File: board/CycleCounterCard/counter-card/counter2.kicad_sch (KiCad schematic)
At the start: 19 parts, among them J1 Bus_Hydra_8bit, J2 74F86, J3 74F86, J4 74F86, J5 74F86, U1 74F191, U13 74F573, U2 74F573, U21 74F573, U22 74F191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

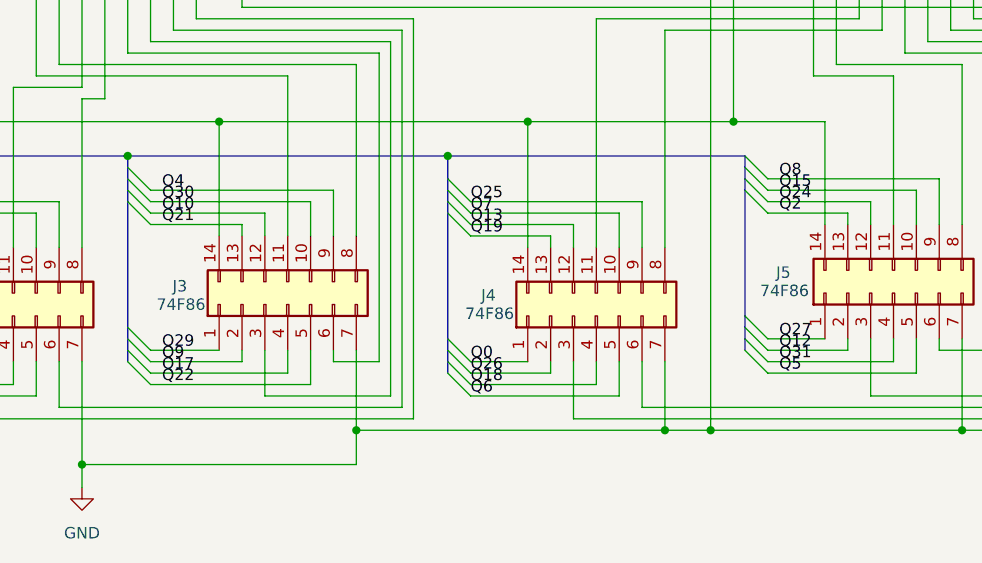
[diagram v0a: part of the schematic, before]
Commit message: Counter card updated to 4-layer to make production simpler and cheaper.  Production V1 model.
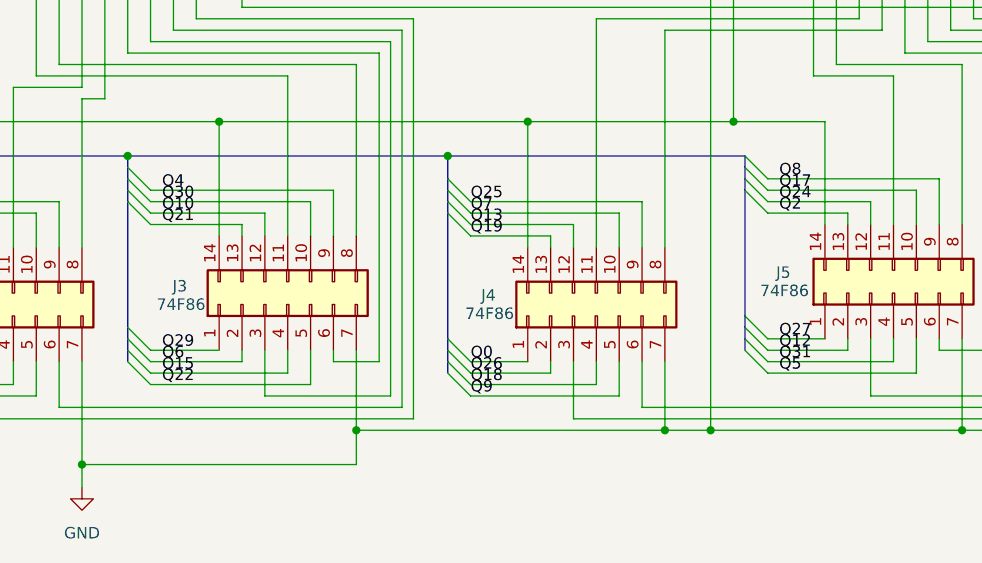
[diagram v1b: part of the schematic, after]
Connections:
- net Q15: now also J3.4 (Pin_4); no longer J5.10 (Pin_10)
- net Q17: now also J5.10 (Pin_10); no longer J3.4 (Pin_4)
- net Q6: now also J3.2 (Pin_2); no longer J4.5 (Pin_5)
- net Q9: now also J4.5 (Pin_5); no longer J3.2 (Pin_2)
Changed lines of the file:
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@@
 		)
 	)
-	(label "Q17"
+	(label "Q15"
 		(at 114.3 163.83 0)
 		(effects
@@
 		)
 	)
-	(label "Q9"
+	(label "Q6"
 		(at 114.3 162.56 0)
 		(effects
@@
 		)
 	)
-	(label "Q15"
+	(label "Q17"
 		(at 182.88 143.51 0)
 		(effects
@@
 		)
 	)
-	(label "Q6"
+	(label "Q9"
 		(at 148.59 166.37 0)
 		(effects
